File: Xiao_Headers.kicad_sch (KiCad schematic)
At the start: 11 parts, among them SW1 Button, U2 ESP32-C3-WROOM-02, U3 TSL25911FN

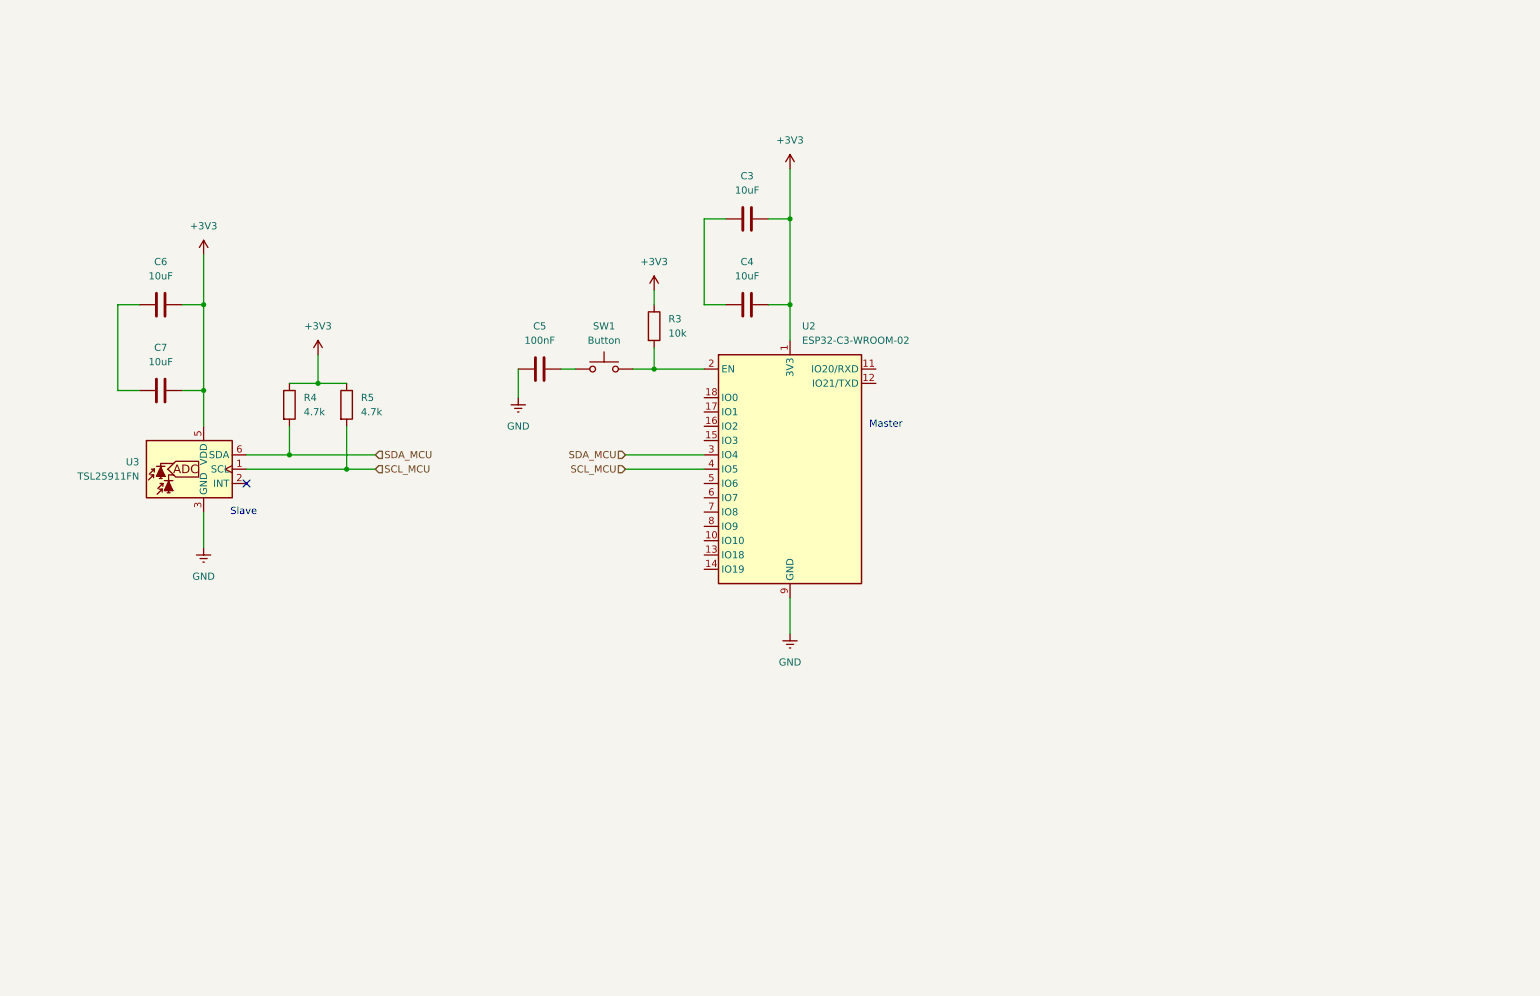
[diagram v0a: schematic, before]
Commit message: Updated Schematic
- Add SHT4X schematic
- Add power rail from 12V DC jack
- Add USB C Schematic (Incomplete)

Note: MCU Minimum System not done
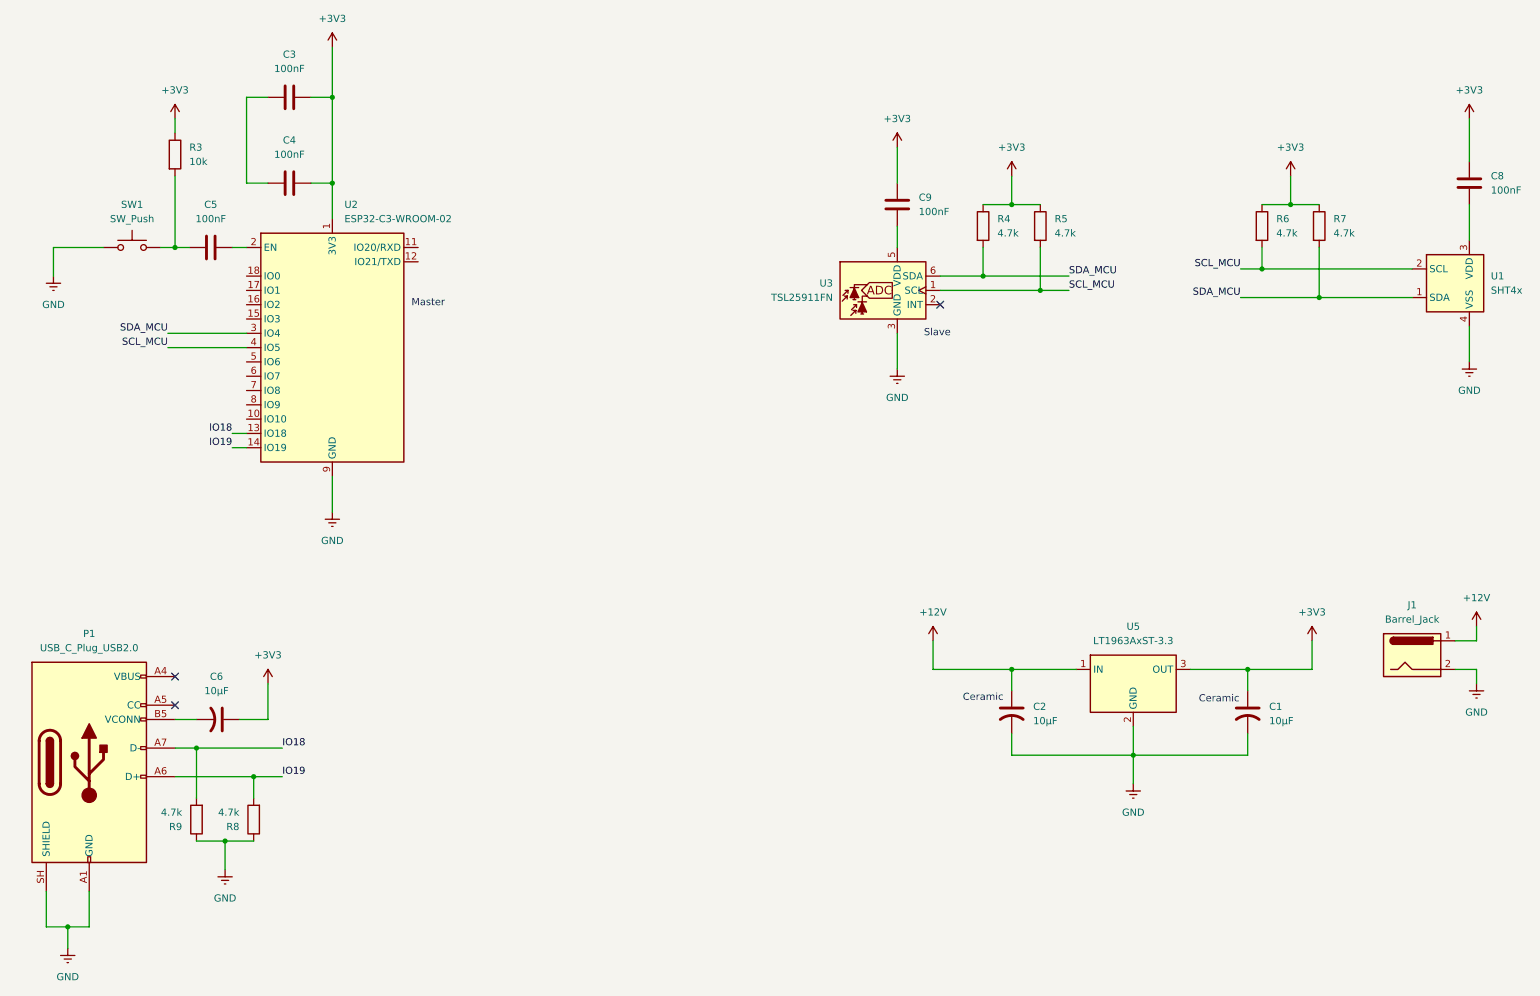
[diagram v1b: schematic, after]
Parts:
- removed C6, C7: 10uF, symbol Device:C
- added C1, C2, C6: 10μF, symbol Device:C_US
- added C8, C9: 100nF, symbol Device:C
- added J1: Barrel_Jack, symbol Connector:Barrel_Jack
- added P1: USB_C_Plug_USB2.0, symbol Connector:USB_C_Plug_USB2.0
- added R6, R7, R8, R9: 4.7k, symbol Device:R
- added U1: SHT4x, Sensor_Humidity:Sensirion_DFN-4_1.5x1.5mm_P0.8mm_SHT4x_NoCentralPad, symbol Sensor_Humidity:SHT4x
- added U5: LT1963AxST-3.3, Package_TO_SOT_SMD:SOT-223-3_TabPin2, symbol Regulator_Linear:LT1963AxST-3.3
- C3, C4: value 10uF -> 100nF
- SW1: value Button -> SW_Push
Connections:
- net +3V3: now also C1.1, C6.1, C8.2, C9.2, R6.1, R7.1, U5.3 (OUT); no longer U3.5 (VDD)
- net GND: now also SW1.1, C1.2, C2.2, J1.2, P1.A1 (GND), P1.A12 (GND), P1.B1 (GND), P1.B12 (GND), P1.SH (SHIELD), R8.1, R9.1, U1.4 (VSS), U5.2 (GND); no longer C5.1
- net SCL_MCU: now also R6.2, U1.2 (SCL)
- net SDA_MCU: now also R7.2, U1.1 (SDA)
- net at R3.2, SW1.2: now also C5.1; no longer U2.2 (EN)
- net at C5.2: now also U2.2 (EN); no longer SW1.1
- net IO18: now reaches U2.13 (IO18)
- net IO18: now also P1.A7 (D-), R9.2
- net IO19: now reaches U2.14 (IO19)
- net IO19: now also P1.A6 (D+), R8.2
- new net: C6.2, P1.B5 (VCONN)
- new net: C9.1, U3.5 (VDD)
- new net: P1.A4 (VBUS), P1.A9 (VBUS), P1.B4 (VBUS), P1.B9 (VBUS)
- new net: C8.1, U1.3 (VDD)
- new net +12V: C2.1, J1.1, U5.1 (IN)
- no-connect marks 1 -> 3
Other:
- note added: "Ceramic"
- moved on the sheet: C3, C4, R3, R4, R5, U2, U3

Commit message: Finalize MCU Minsys
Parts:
- added C7: 100nF, symbol Device:C
- added R10, R11: 10k, symbol Device:R
- added SW2: SW_Push, symbol Switch:SW_Push
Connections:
- net +3V3: now also R10.1, R11.1
- net GND: now also SW2.2
- net at C5.1, SW1.2: no longer R3.2
- net at U2.16 (IO2): now also R10.2
- net at C5.2, U2.2 (EN): now also R3.2
- net at U2.8 (IO9): now also C7.2, R11.2
- new net: C7.1, SW2.1
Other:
- moved on the sheet: R3, SW1
